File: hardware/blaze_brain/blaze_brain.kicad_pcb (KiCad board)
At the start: 2 copper layers, 70 x 70 mm, 2 parts, among them J2 Conn_01x30_Pin, J3 Conn_01x30_Socket

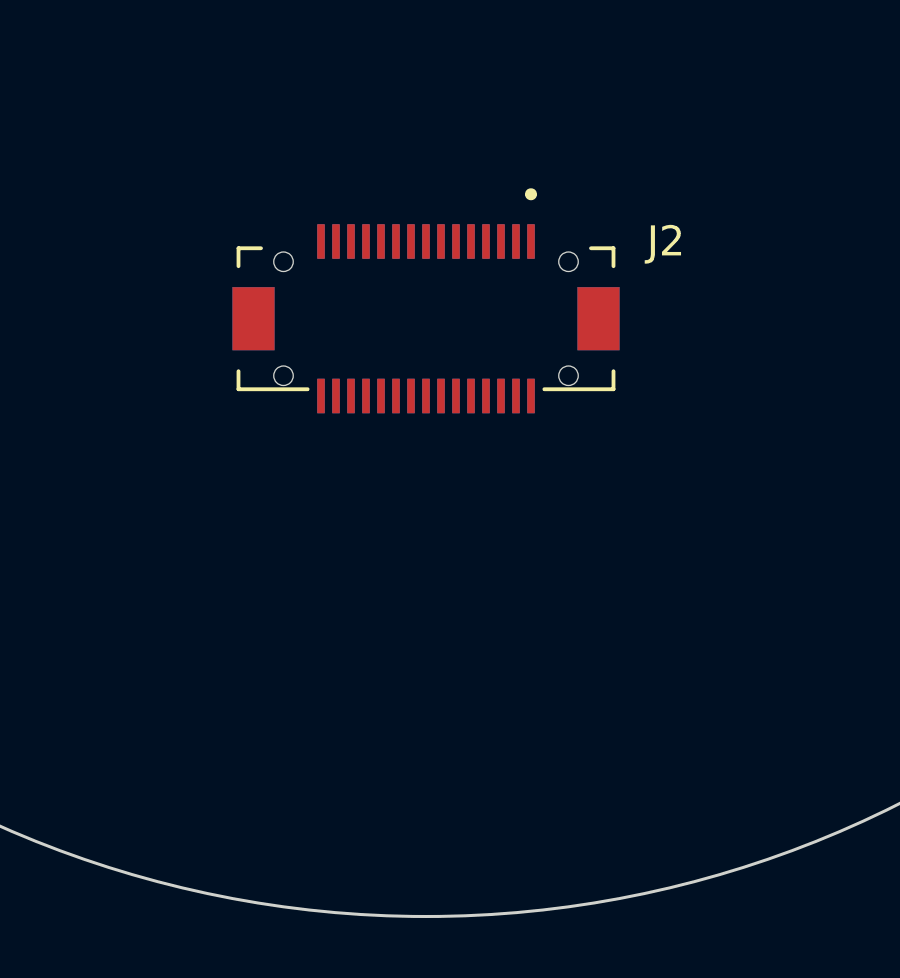
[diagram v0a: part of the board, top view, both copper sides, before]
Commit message: Brought in PCB template
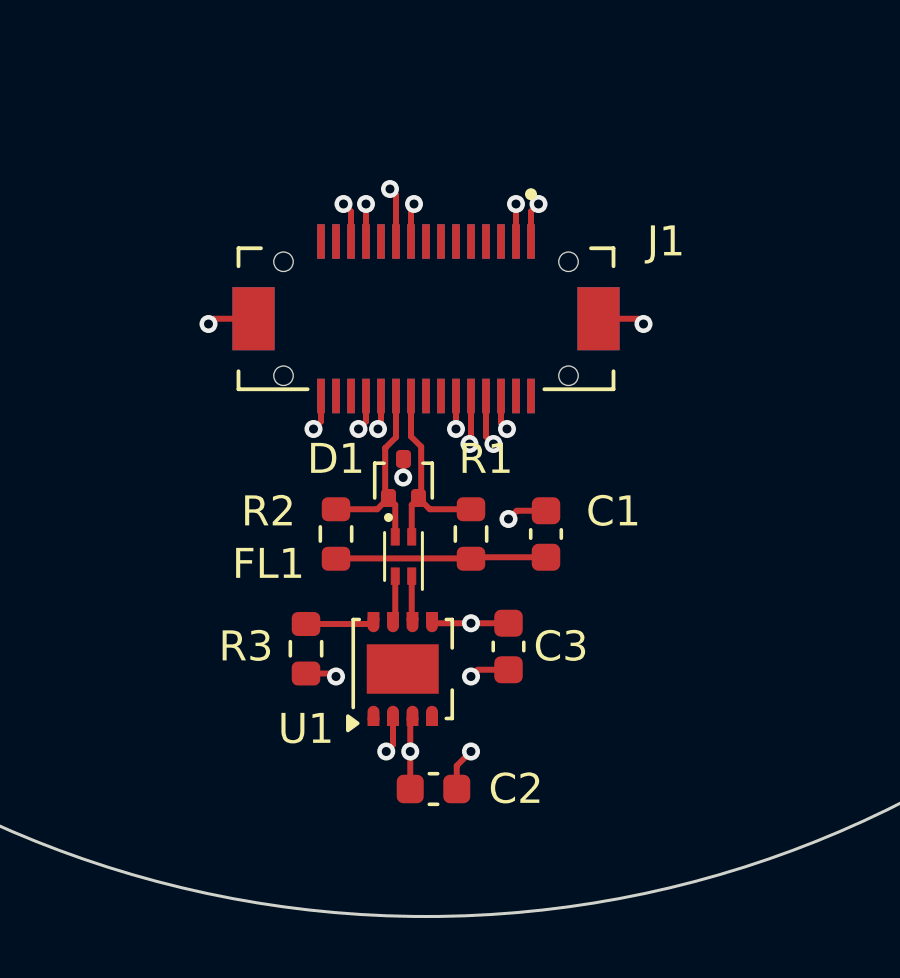
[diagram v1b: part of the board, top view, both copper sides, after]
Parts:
- added C1: 4.7nF, Capacitor_SMD:C_0603_1608Metric, F.Cu at (152.5, 127.8)
- added C2: 0.1uF, Capacitor_SMD:C_0603_1608Metric, F.Cu at (148.8, 136.2)
- added C3: 0.1uF, Capacitor_SMD:C_0603_1608Metric, F.Cu at (151.2, 131.5)
- added D1: ESDCAN03-2BM3Y, Package_TO_SOT_SMD:SOT-416, F.Cu at (147.8, 125.9)
- added FL1: Choke, Inductor_SMD:L_CommonModeChoke_Coilcraft_0603USB, F.Cu at (147.8, 128.5)
- added R1: 60, Resistor_SMD:R_0603_1608Metric, F.Cu at (150.0, 127.8)
- added R2: 60, Resistor_SMD:R_0603_1608Metric, F.Cu at (145.5, 127.8)
- added R3: 10K, Resistor_SMD:R_0603_1608Metric, F.Cu at (144.5, 131.6)
- added U1: TCAN1044VDDFR, Package_SON:Texas_S-PVSON-N8, F.Cu at (147.7, 132.2)
- J1: renamed from J2; value Conn_01x30_Pin -> FrontInterconnect
- J2: renamed from J3; value Conn_01x30_Socket -> RearInterconnect
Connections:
- J1 pad 1: Net-(J2-Pin_1) -> GND
- J1 pad 10: Net-(J2-Pin_10) -> +3V3
- J1 pad 11: +5V -> /PPS
- J1 pad 12: +3V3 -> GND
- J1 pad 13: /PPS -> GND
- J1 pad 14: GND -> Net-(J1-Pin_14)
- J1 pad 15: GND -> Net-(J1-Pin_15)
- J1 pad 16: Net-(J2-Pin_16) -> +3V3
- J1 pad 18: +3V3 -> Net-(J1-Pin_18)
- J1 pad 19: Net-(J2-Pin_19) -> GND
- J1 pad 2: Net-(J2-Pin_2) -> GND
- J1 pad 20: Net-(J2-Pin_20) -> GND
- J1 pad 21: GND -> /CANH
- J1 pad 22: GND -> /CANL
- J1 pad 23: /CANL -> Net-(J1-Pin_23)
- J1 pad 24: /CANH -> Net-(J1-Pin_24)
- J1 pad 25: Net-(J2-Pin_25) -> +5V
- J1 pad 26: Net-(J2-Pin_26) -> +5V
- J1 pad 27: +5V -> +3V3
- J1 pad 28: +5V -> +3V3
- J1 pad 29: +3V3 -> Net-(J1-Pin_29)
- J1 pad 3: GND -> /TX_RADIO
- J1 pad 30: +3V3 -> Net-(J1-Pin_30)
- J1 pad 4: GND -> /RX_RADIO
- J1 pad 5: /TX_RADIO -> Net-(J1-Pin_5)
- J1 pad 6: /RX_RADIO -> /ARM
- J1 pad 8: /ARM -> Net-(J1-Pin_8)
- J1 pad 9: Net-(J2-Pin_9) -> +5V
- J1 pad S1: (no net) -> GND
- J1 pad S2: (no net) -> GND
- J2 pad 1: +3V3 -> Net-(J1-Pin_30)
- J2 pad 10: GND -> /CANH
- J2 pad 11: Net-(J2-Pin_20) -> GND
- J2 pad 12: Net-(J2-Pin_19) -> GND
- J2 pad 13: +3V3 -> Net-(J1-Pin_18)
- J2 pad 15: Net-(J2-Pin_16) -> +3V3
- J2 pad 16: GND -> Net-(J1-Pin_15)
- J2 pad 17: GND -> Net-(J1-Pin_14)
- J2 pad 18: /PPS -> GND
- J2 pad 19: +3V3 -> GND
- J2 pad 2: +3V3 -> Net-(J1-Pin_29)
- J2 pad 20: +5V -> /PPS
- J2 pad 21: Net-(J2-Pin_10) -> +3V3
- J2 pad 22: Net-(J2-Pin_9) -> +5V
- J2 pad 23: /ARM -> Net-(J1-Pin_8)
- J2 pad 25: /RX_RADIO -> /ARM
- J2 pad 26: /TX_RADIO -> Net-(J1-Pin_5)
- J2 pad 27: GND -> /RX_RADIO
- J2 pad 28: GND -> /TX_RADIO
- J2 pad 29: Net-(J2-Pin_2) -> GND
- J2 pad 3: +5V -> +3V3
- J2 pad 30: Net-(J2-Pin_1) -> GND
- J2 pad 4: +5V -> +3V3
- J2 pad 5: Net-(J2-Pin_26) -> +5V
- J2 pad 6: Net-(J2-Pin_25) -> +5V
- J2 pad 7: /CANH -> Net-(J1-Pin_24)
- J2 pad 8: /CANL -> Net-(J1-Pin_23)
- J2 pad 9: GND -> /CANL
- J2 pad S1: (no net) -> GND
- J2 pad S2: (no net) -> GND
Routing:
- net +5V: track 0.00 -> 26.1 mm, vias 0 -> 4
- net GND: track 0.00 -> 16.8 mm, vias 0 -> 13
- net +3V3: track 0.00 -> 9.52 mm, vias 0 -> 6
- net Net-(C1-Pad1): track 0.00 -> 7.28 mm
- net /CANH: track 0.00 -> 6.89 mm
- net /CANL: track 0.00 -> 6.87 mm
- net /CAN_STB: track 0.00 -> 2.27 mm
- net Net-(U1-CANL): track 0.00 -> 1.59 mm
- net Net-(U1-CANH): track 0.00 -> 1.58 mm
- added copper zone on In1.Cu, net +3V3
- added copper zone on In2.Cu, net GND
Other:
- copper layers 2 -> 4

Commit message: Initial component positioning
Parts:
- added C5: 47uF, Capacitor_SMD:C_0603_1608Metric, F.Cu at (156.4, 105.0)
- added C6: 1uF, Capacitor_SMD:C_0603_1608Metric, F.Cu at (167.4, 88.0)
- added C7: 0.1uF, Capacitor_SMD:C_0603_1608Metric, F.Cu at (163.6, 110.5)
- added D1: WS2812B, LED_SMD:LED_WS2812B_PLCC4_5.0x5.0mm_P3.2mm, F.Cu at (167.3, 82.9)
- added J4: Micro_SD_Card, Blaze_Library:CONN_47219-2001_MOL, F.Cu at (174.3, 105.8)
- added J5: Conn_01x03_Pin, Connector_PinHeader_2.54mm:PinHeader_1x03_P2.54mm_Vertical, F.Cu at (160.0, 75.2)
- added Q2: FDN340P, Package_TO_SOT_SMD:SOT-23, F.Cu at (162.8, 104.8)
- added R1: 47k, Resistor_SMD:R_0603_1608Metric, F.Cu at (154.3, 105.0)
- added R2: 100k, Resistor_SMD:R_0603_1608Metric, F.Cu at (158.5, 105.0)
- added R3: 10K, Resistor_SMD:R_0603_1608Metric, F.Cu at (143.0, 93.7)
- added U3: Teensy4.0, Blaze_Library:Teensy40, F.Cu at (133.3, 105.4)
- added U4: W25N02KVZEIR, Package_SON:WSON-8-1EP_6x5mm_P1.27mm_EP3.4x4.3mm, F.Cu at (158.5, 111.5)
- renumbered D1 to D2, R1 to R4, R2 to R5, R3 to R6
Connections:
- D2 pad 1: /CANH -> /CANL
- D2 pad 2: /CANL -> /CANH

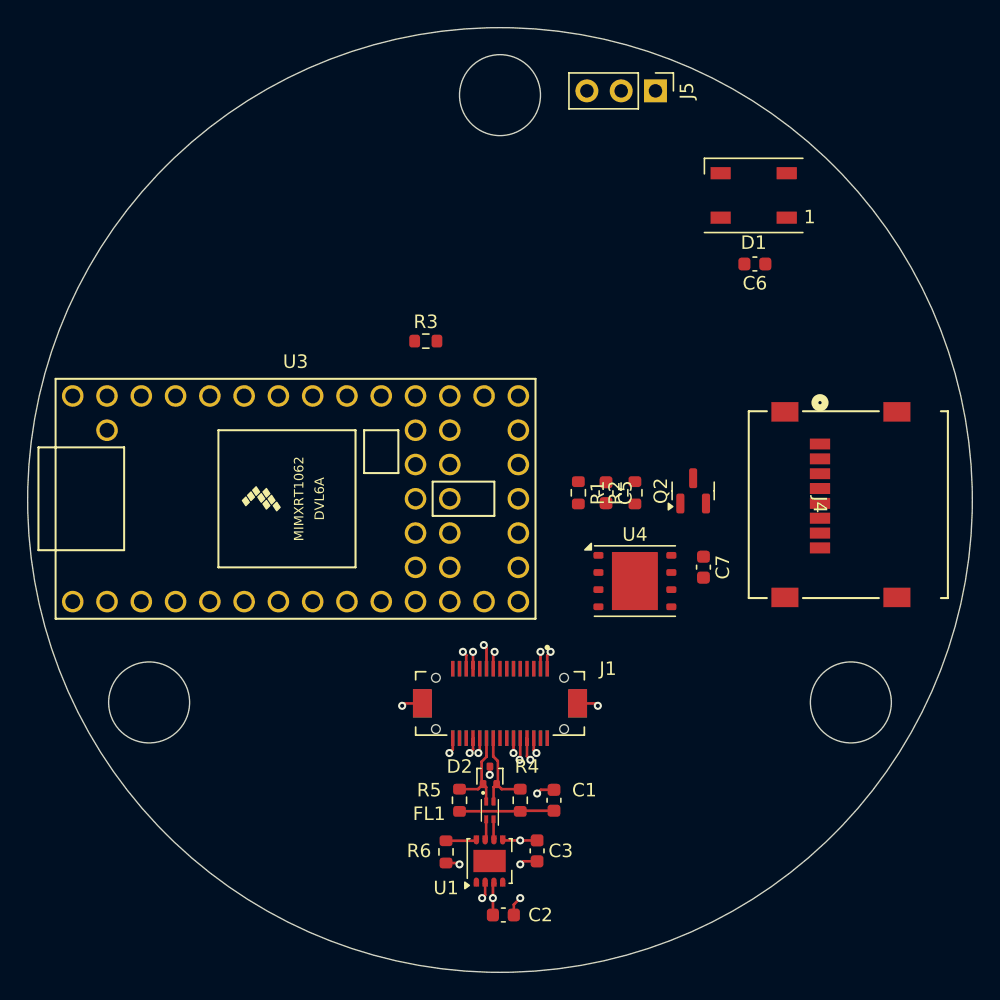
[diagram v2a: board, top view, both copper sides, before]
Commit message: Routed board
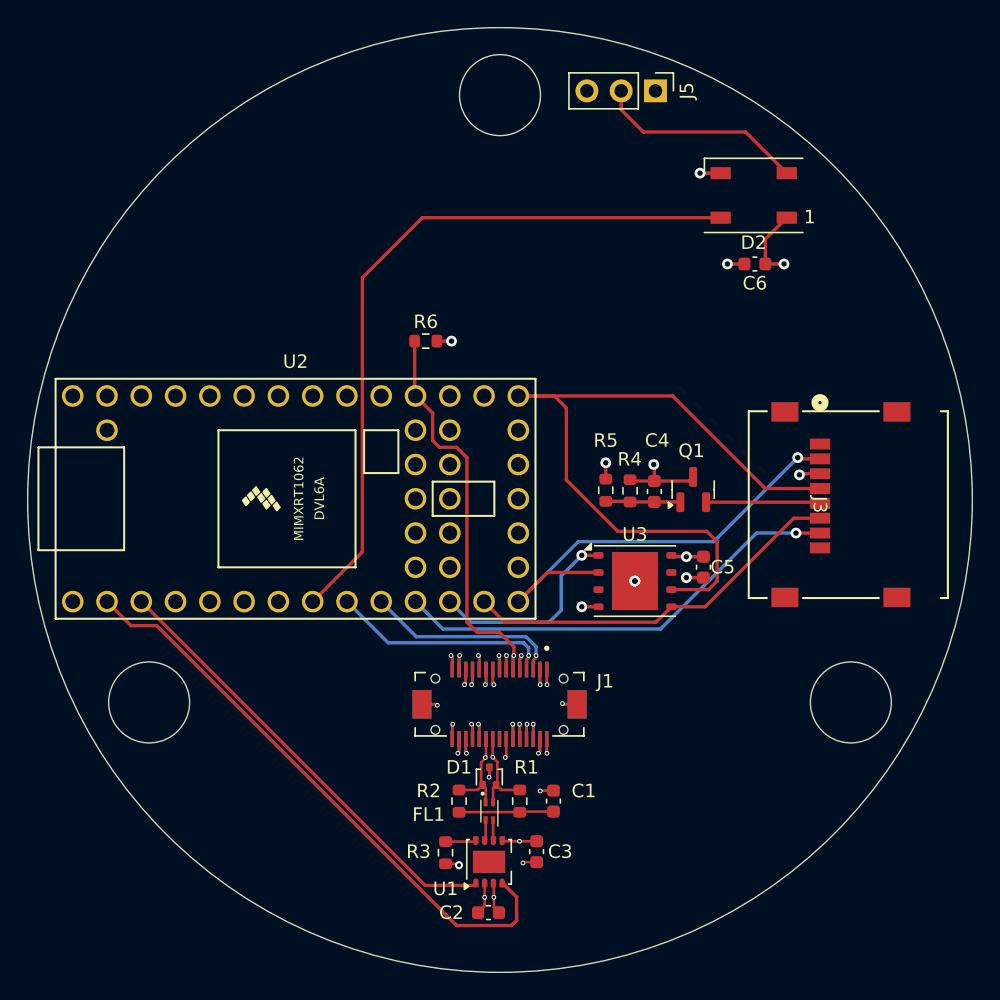
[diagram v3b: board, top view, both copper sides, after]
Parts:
- removed the D2 at (147.8, 125.9)
- removed the R4 at (150.0, 127.8)
- removed the R5 at (145.5, 127.8)
- removed the R6 at (144.5, 131.6)
- added D1: ESDCAN03-2BM3Y, Package_TO_SOT_SMD:SOT-416, F.Cu at (147.7, 126.0)
- added R1: 60, Resistor_SMD:R_0603_1608Metric, F.Cu at (150.0, 127.8)
- added R2: 60, Resistor_SMD:R_0603_1608Metric, F.Cu at (145.5, 127.8)
- added R3: 10K, Resistor_SMD:R_0603_1608Metric, F.Cu at (144.5, 131.6)
- moved R4 3.84 mm to (158.1, 104.8)
- moved C4 3.58 mm to (159.9, 104.9)
- moved R5 2.17 mm to (156.3, 104.8)
- moved C2 1.11 mm to (147.7, 136.1), turned to 180 degrees
- moved Q1 0.10 mm to (162.8, 104.7)
- moved C1 0.07 mm to (152.5, 127.8)
- moved C3 0.07 mm to (151.2, 131.6)
- moved FL1 0.07 mm to (147.7, 128.6)
- moved U1 0.07 mm to (147.7, 132.3)
- moved J1 0.07 mm to (148.5, 120.6)
- moved J2 0.07 mm to (148.5, 120.6)
- renumbered C5 to C4, C7 to C5, D1 to D2, J4 to J3, Q2 to Q1, R1 to R4, R2 to R5, R3 to R6, U3 to U2, U4 to U3
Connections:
- J1 pad 3: /TX_RADIO -> /RX_RADIO
- J1 pad 4: /RX_RADIO -> /TX_RADIO
- J2 pad 27: /RX_RADIO -> /TX_RADIO
- J2 pad 28: /TX_RADIO -> /RX_RADIO
- U2 pad 10: unconnected-(U3-8_TX2_IN1-Pad10) -> /RX_RADIO
- U2 pad 9: unconnected-(U3-7_RX2_OUT1A-Pad9) -> /TX_RADIO
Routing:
- net +5V: track 26.1 -> 146.5 mm, vias 4 -> 5
- net /SCK: track 0.00 -> 54.1 mm
- net /LED_DOUT: track 0.00 -> 53.9 mm
- net /CANRX: track 0.00 -> 44.3 mm
- net /CS_SD: track 0.00 -> 33.8 mm, vias 0 -> 1
- net /MISO: track 0.00 -> 33.6 mm, vias 0 -> 1
- net /CANTX: track 0.00 -> 33.5 mm
- net /ARM: track 0.00 -> 30.2 mm, vias 0 -> 1
- net /MOSI: track 0.00 -> 28.7 mm
- net /TX_RADIO: track 0.00 -> 17.7 mm, vias 0 -> 1
- net /RX_RADIO: track 0.00 -> 15.8 mm, vias 0 -> 1
- net GND: track 16.8 -> 32.4 mm, vias 13 -> 21
- net Net-(D2-DOUT): track 0.00 -> 15.6 mm
- net /CS_FLASH: track 0.00 -> 15.2 mm, vias 0 -> 1
- net +3V3: track 9.52 -> 21.1 mm, vias 6 -> 8
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
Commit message: Updated routing, rounded tracks
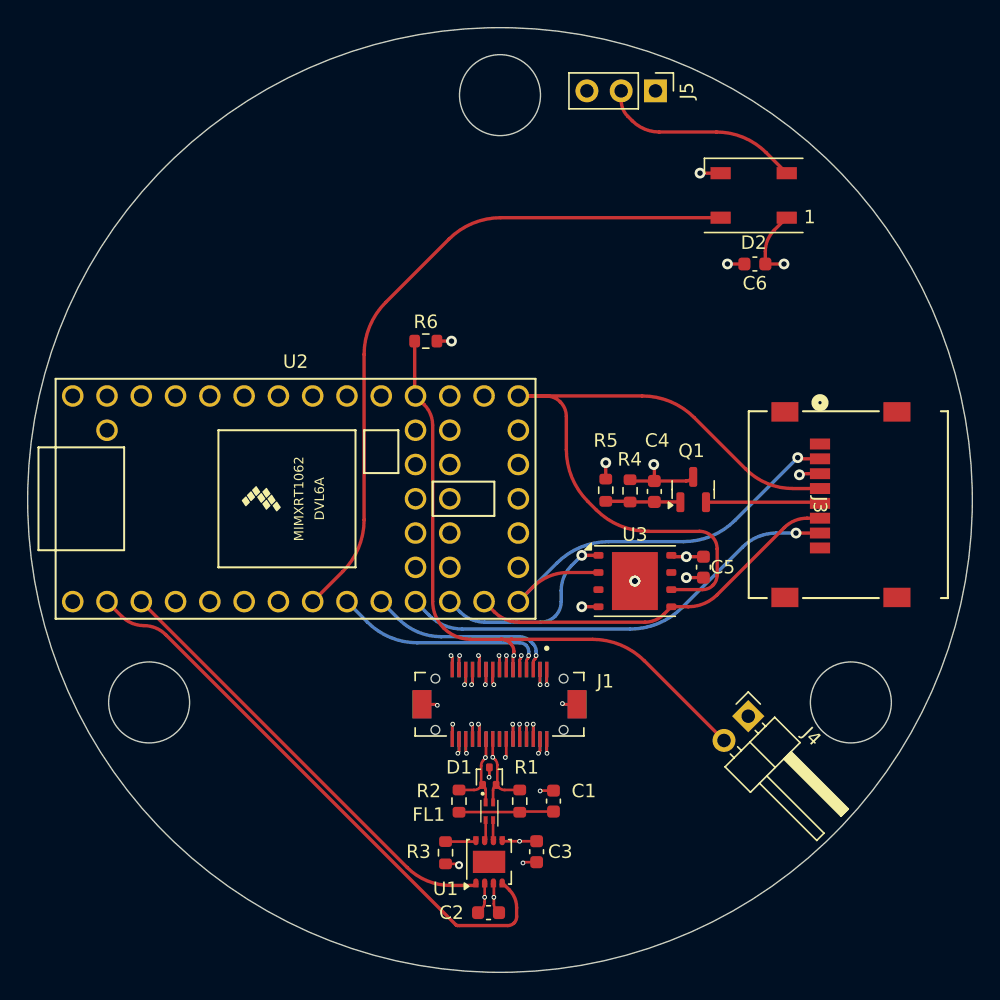
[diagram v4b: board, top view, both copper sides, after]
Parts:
- added J4: Conn_01x02, Connector_PinHeader_2.54mm:PinHeader_1x02_P2.54mm_Horizontal, F.Cu at (166.9, 121.5)
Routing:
- net /ARM: track 30.2 -> 49.9 mm
- net +5V: track 146.5 -> 142.7 mm
- net /LED_DOUT: track 53.9 -> 51.0 mm
- net /SCK: track 54.1 -> 52.7 mm
- net /CANRX: track 44.3 -> 43.6 mm
- net /MISO: track 33.6 -> 32.9 mm
- net /CS_SD: track 33.8 -> 33.2 mm
